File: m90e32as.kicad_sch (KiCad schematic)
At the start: 72 parts, among them J3 MX15EDGRHC-3.5-2x03P, J4 MX15EDGKNH-3.5-2x03P, U10 ATM90E32AS-AU-R, U11 K3-2268P, U8 DB126V-5.0-2P-BK-P, U9 DB126V-5.0-2P-BK-P, Y1 ABM8G-16.384MHZ-18-D2Y-T

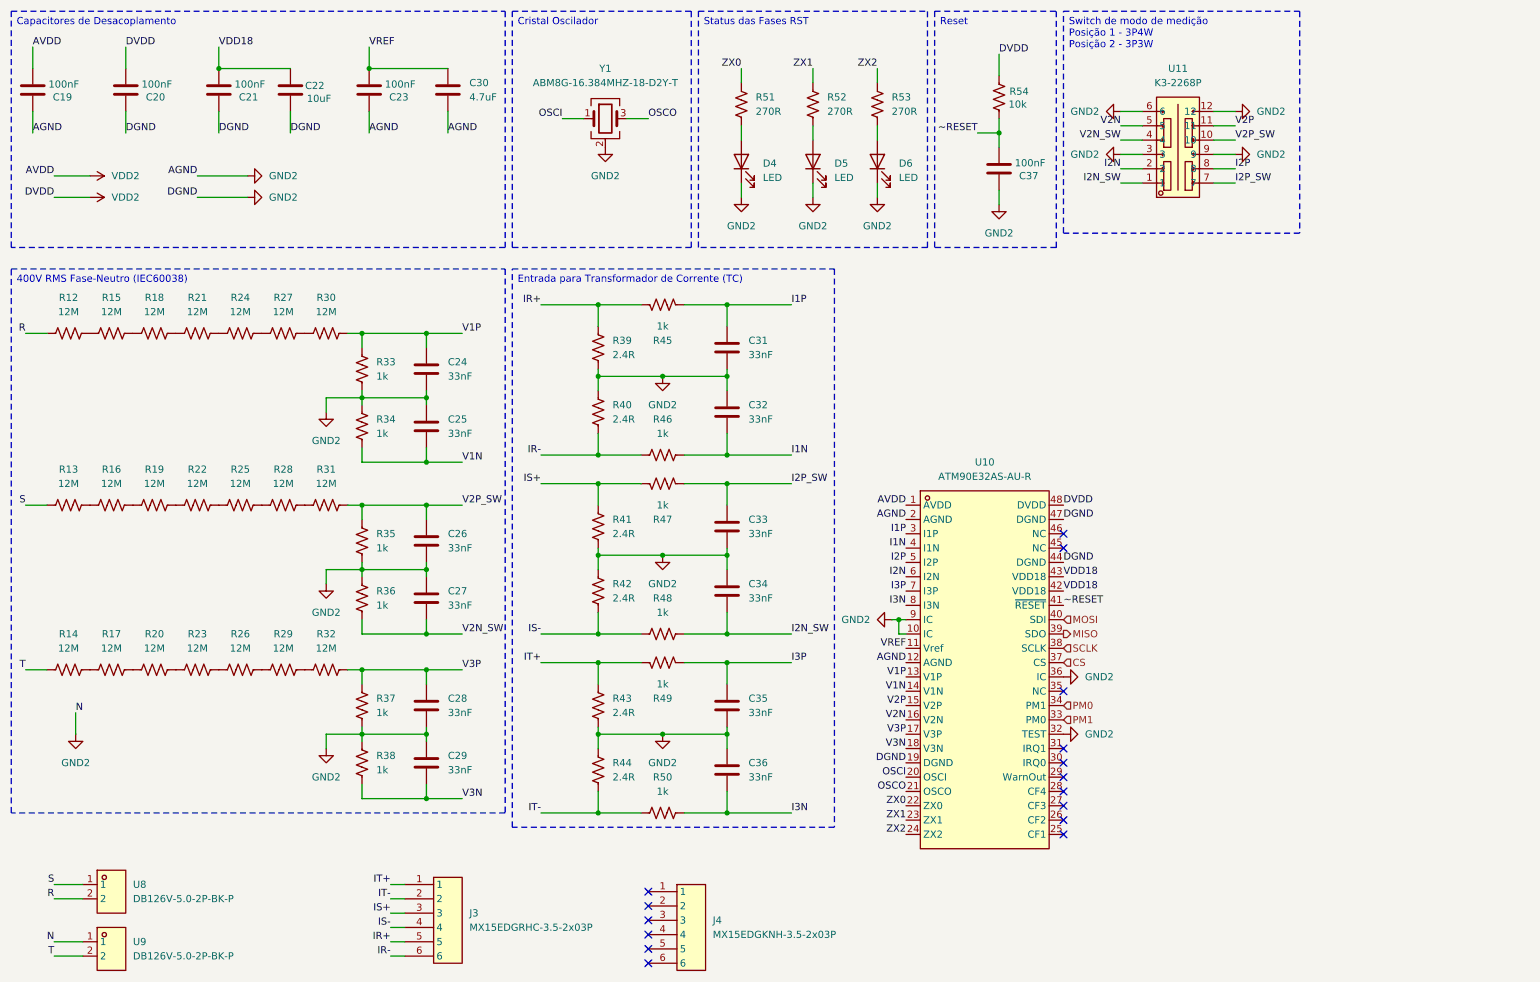
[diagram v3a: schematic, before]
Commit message: Migra componentes das bibliotecas LCSC locais para pecas JLCPCB
Troca os part numbers para casar com o estoque da JLCPCB e com o
catalogo PCBA Basic, eliminando a biblioteca local que era importada
via easyeda2kicad.

- Remove libraries/ (simbolos, footprints e modelos 3D importados) e o
  script import_lcsc_component.sh
- Adiciona o plugin JLCPCB (jlcpcb/project.db) e os scripts auxiliares
  fix_jlcpcb_tools_deps.sh e generate_ibom.sh
- Atualiza as cinco folhas do esquematico, o PCB e as regras de projeto

O PCB fica em estado intermediario: os componentes novos ainda precisam
ser reposicionados e as trilhas refeitas.

Co-Authored-By: Claude Opus 5 (1M context) <noreply@anthropic.com>
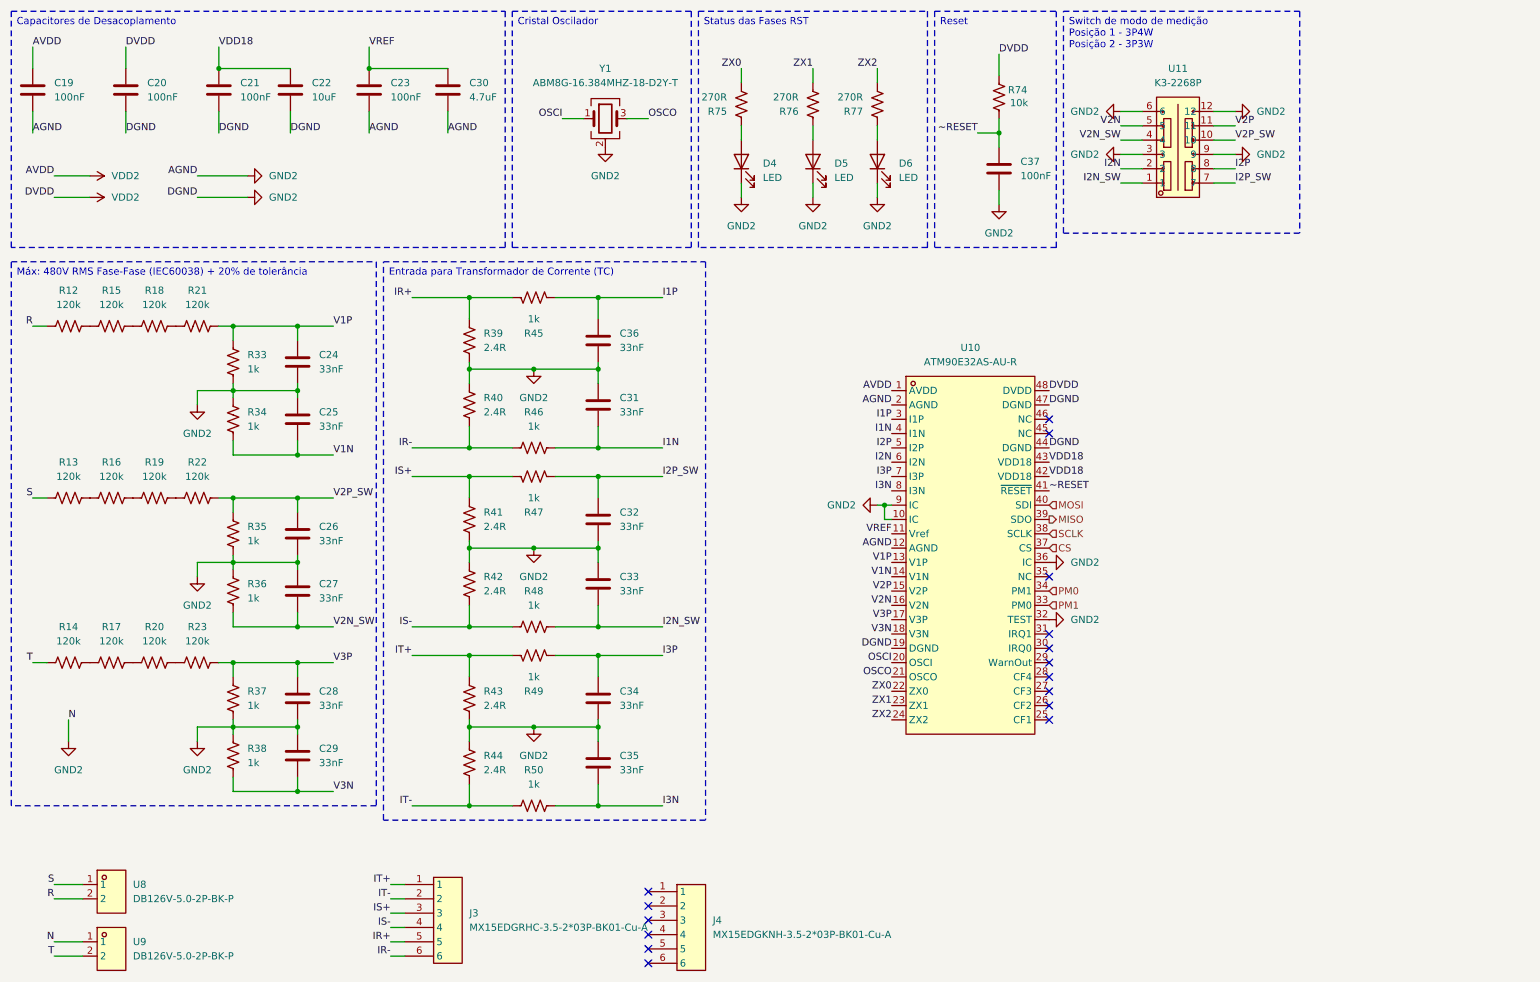
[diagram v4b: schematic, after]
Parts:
- removed R24, R25, R26, R27, R28, R29, R30, R31, R32: 12M, Resistor_SMD:R_1206_3216Metric, symbol Device:R_US
- removed R51, R52, R53: 270R, Resistor_SMD:R_0402_1005Metric, symbol Device:R_US
- removed R54: 10k, Resistor_SMD:R_0402_1005Metric, symbol Device:R_US
- added R74: 10k, Resistor_SMD:R_0402_1005Metric, symbol Device:R_US
- added R75, R76, R77: 270R, Resistor_SMD:R_0603_1608Metric, symbol Device:R_US
- C19, C20, C21, C23, C37: footprint Capacitor_SMD:C_0201_0603Metric -> Capacitor_SMD:C_0402_1005Metric; JLCPCB Part # (none) -> C1525; LCSC Part # C7393837 -> (none); MPN TCC0201X7R104K100ZT -> CL05B104KO5NNNC
- C22: footprint Capacitor_SMD:C_0603_1608Metric -> Capacitor_SMD:C_0402_1005Metric; JLCPCB Part # (none) -> C15525; LCSC Part # C6119842 -> (none); MPN CGA0603X5R106K100JT -> CL05A106MQ5NUNC
- C24, C25, C26, C27, C28, C29, C31, C32, C33, C34, C35, C36: footprint Capacitor_SMD:C_0402_1005Metric -> Capacitor_SMD:C_0805_2012Metric; JLCPCB Part # (none) -> C1739; LCSC Part # C48543509 -> (none); MPN TCC0402X7R333J500AT -> 0805B333K500NT
- C30: JLCPCB Part # (none) -> C23733; LCSC Part # C22399610 -> (none); MPN CGA0402X5R475K6R3GT -> CL05A475MP5NRNC
- D4, D5, D6: JLCPCB Part # (none) -> C2994781; LCSC Part # C2994781 -> (none)
- J3: value MX15EDGRHC-3.5-2x03P -> MX15EDGRHC-3.5-2*03P-BK01-Cu-A; JLCPCB Part # (none) -> C49142489; LCSC Part # C49142489 -> (none)
- J4: value MX15EDGKNH-3.5-2x03P -> MX15EDGKNH-3.5-2*03P-BK01-Cu-A; JLCPCB Part # (none) -> C49142469; LCSC Part # C49142469 -> (none)
- R12, R13, R14, R15, R16, R17, R18, R19, R20, R21, R22, R23: value 12M -> 120k; footprint Resistor_SMD:R_1206_3216Metric -> Resistor_THT:R_Axial_DIN0207_L6.3mm_D2.5mm_P10.16mm_Horizontal; JLCPCB Part # (none) -> C119370; LCSC Part # C5126174 -> (none); MPN FRG1206F1205TS -> MF1/4W-120KΩ±1% T
- R33, R34, R35, R36, R37, R38, R45, R46, R47, R48, R49, R50: JLCPCB Part # (none) -> C11702; LCSC Part # C7468310 -> (none); MPN FRP0402F1001TS -> 0402WGF1001TCE
- R39, R40, R41, R42, R43, R44: JLCPCB Part # (none) -> C2998116; LCSC Part # C2683028 -> (none); MPN ARG03BTC2R40 -> FRC0603F2R40TS
- U10: JLCPCB Part # (none) -> C177153; LCSC Part # C177153 -> (none)
- U11: JLCPCB Part # (none) -> C502352; LCSC Part # C502352 -> (none)
- U8, U9: JLCPCB Part # (none) -> C49260677; LCSC Part # C49260677 -> (none)
- Y1: JLCPCB Part # (none) -> C7065080; LCSC Part # C7065080 -> (none)
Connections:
- net GND2: now also C19.2, C20.2, C21.2, C22.2, C23.2, C31.1, C32.2, C33.1, C34.2, C35.1, C36.2, C37.2; no longer C19.1, C20.1, C21.1, C22.1, C23.1, C31.2, C32.1, C33.2, C34.1, C35.2, C36.1, C37.1
- net I1N: now also C31.2; no longer C32.2
- net I1P: now also C36.1; no longer C31.1
- net I2N_SW: now also C33.2; no longer C34.2
- net I2P_SW: now also C32.1; no longer C33.1
- net I3N: now also C35.2; no longer C36.2
- net I3P: now also C34.1; no longer C35.1
- net V1P: now also R21.2
- net V2P_SW: now also R22.2
- net V3P: now also R23.2
- net VDD18: now also C21.1, C22.1; no longer C21.2, C22.2
- net VDD2: now also C19.1, C20.1, R74.2; no longer C19.2, C20.2
- net VREF: now also C23.1; no longer C23.2
- net ZX0: now also R75.1
- net ZX1: now also R76.1
- net ZX2: now also R77.1
- net ~RESET: now also C37.1, R74.1; no longer C37.2
- net at D5.2 (A): now also R76.2
- net at D4.2 (A): now also R75.2
- net at D6.2 (A): now also R77.2
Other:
- moved on the sheet: C24, R12, R33, R39, U10

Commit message: Reintroduz biblioteca local ra5_2022 e atualiza layout/esquematicos
Volta a usar simbolos, footprints e modelos 3D importados via
easyeda2kicad (libraries/) em vez das pecas basicas JLCPCB adotadas no
commit anterior, alem de atualizar o roteamento/posicionamento no PCB
e as cinco folhas do esquematico.

Co-Authored-By: Claude Sonnet 5 <noreply@anthropic.com>
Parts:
- removed U11: K3-2268P, ra5_2022:SW-SMD_12P-L14.9-W4.9_K3-2268P, symbol ra5_2022:K3-2268P
- added JP1, JP2, JP3, JP4: SolderJumper_3_Open, Jumper:SolderJumper-3_P1.3mm_Open_RoundedPad1.0x1.5mm_NumberLabels, symbol Jumper:SolderJumper_3_Open
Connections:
- net GND2: now also JP1.1 (A), JP2.1 (A), JP3.1 (A), JP4.1 (A)
- net I2N: now also JP4.2 (C)
- net I2N_SW: now also JP4.3 (B)
- net I2P: now also JP3.2 (C)
- net I2P_SW: now also JP3.3 (B)
- net IR+: now also J3.1; no longer J3.5
- net IR-: now also J3.2; no longer J3.6
- net IT+: now also J3.5; no longer J3.1
- net IT-: now also J3.6; no longer J3.2
- net V2N: now also JP2.2 (C)
- net V2N_SW: now also JP2.3 (B)
- net V2P: now also JP1.2 (C)
- net V2P_SW: now also JP1.3 (B)
